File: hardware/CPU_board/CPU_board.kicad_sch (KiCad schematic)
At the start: 109 parts, among them J1 TF TF-018 1.5mm, J2 SOUTH, J3 NORTH, J4 Conn_01x6_Male, J5 Conn_01x03, J6 JTAG, J8 Conn_01x10_Male, U1 EA3036A, U2 W25Q32JVZPIQ, U3 D1s-eLQFP128, U4 PAD30, U5 PAD30, U6 PAD30, U7 PAD30, U8 PAD30, U9 PAD30, X1 24MHz, X2 32.768KHz

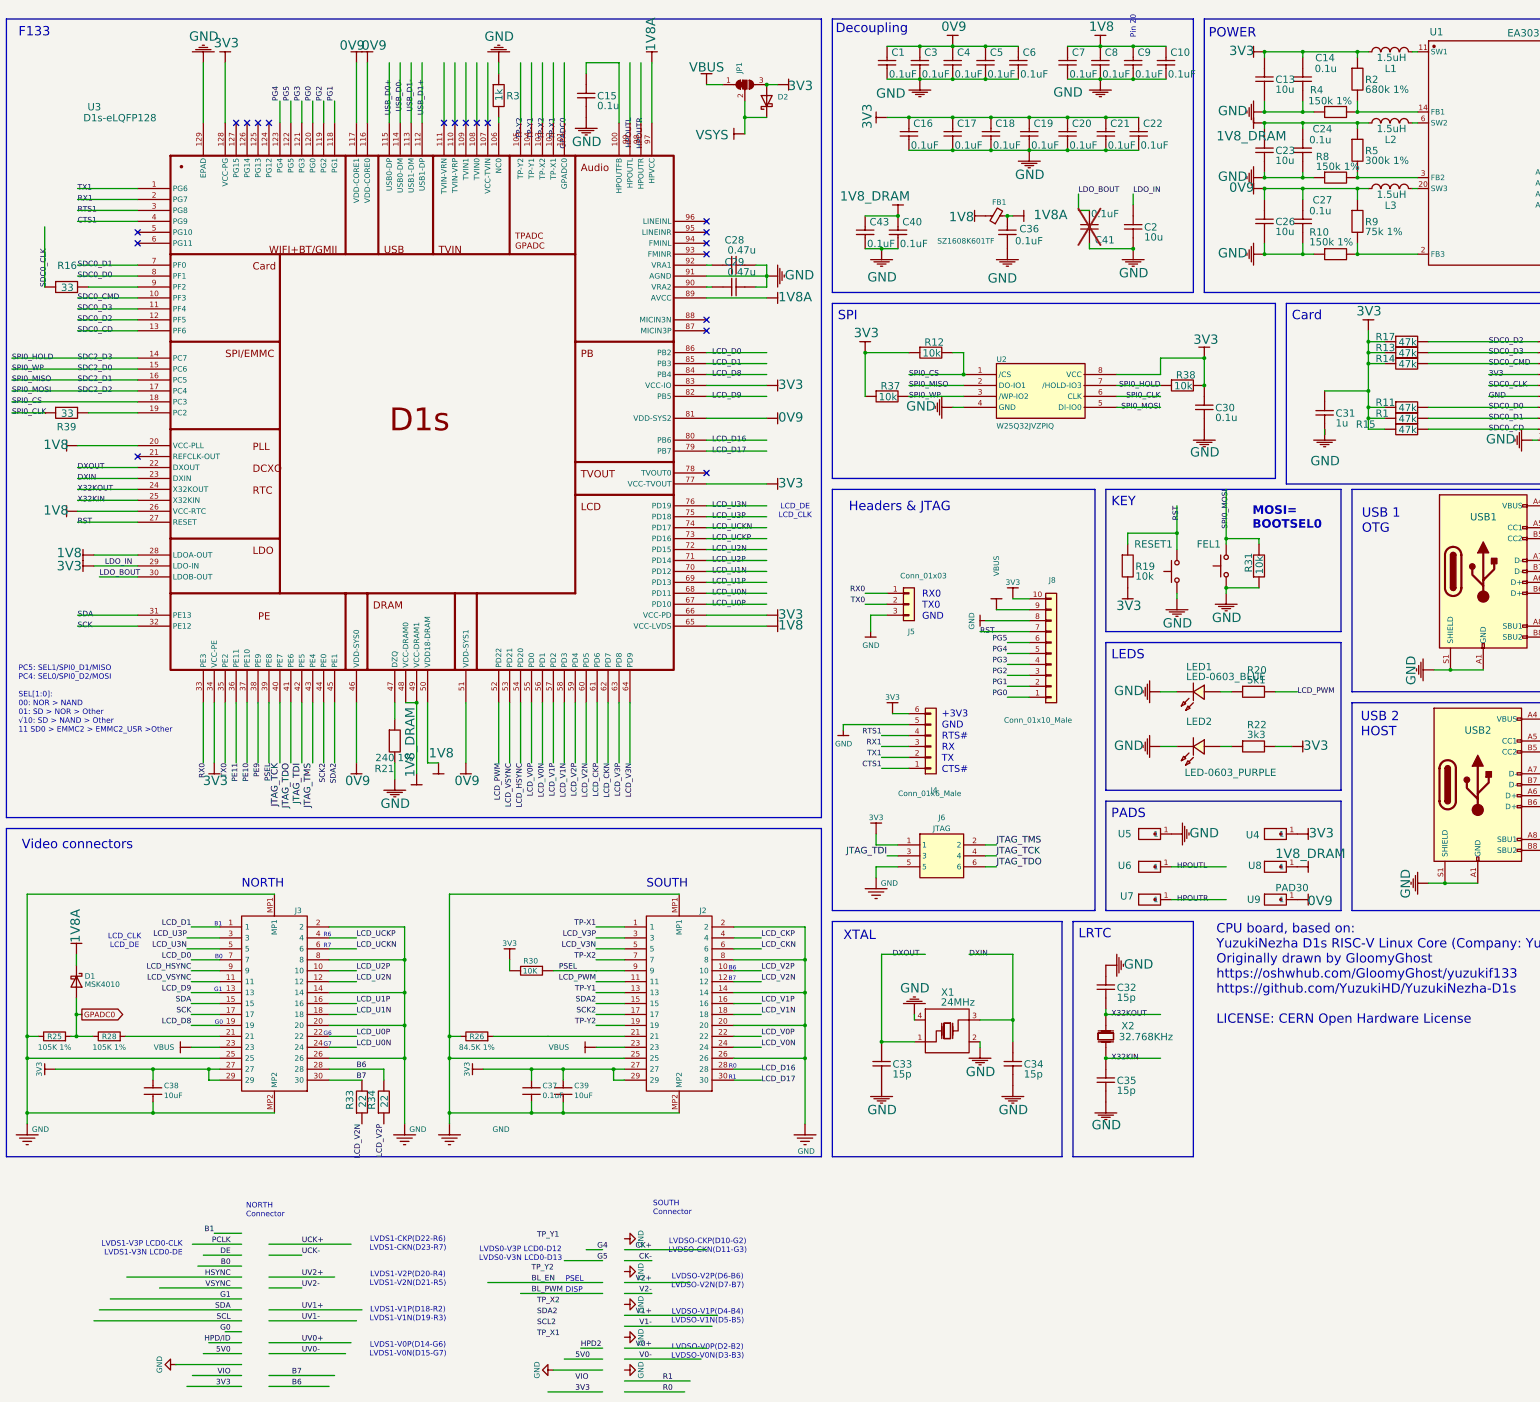
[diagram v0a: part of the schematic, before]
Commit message: fixed mixup of pins G5/G4 (3rd diff pair ODD) and DE/PCLK (3rd diff pair EVEN), now with correct polarity for diff pairs
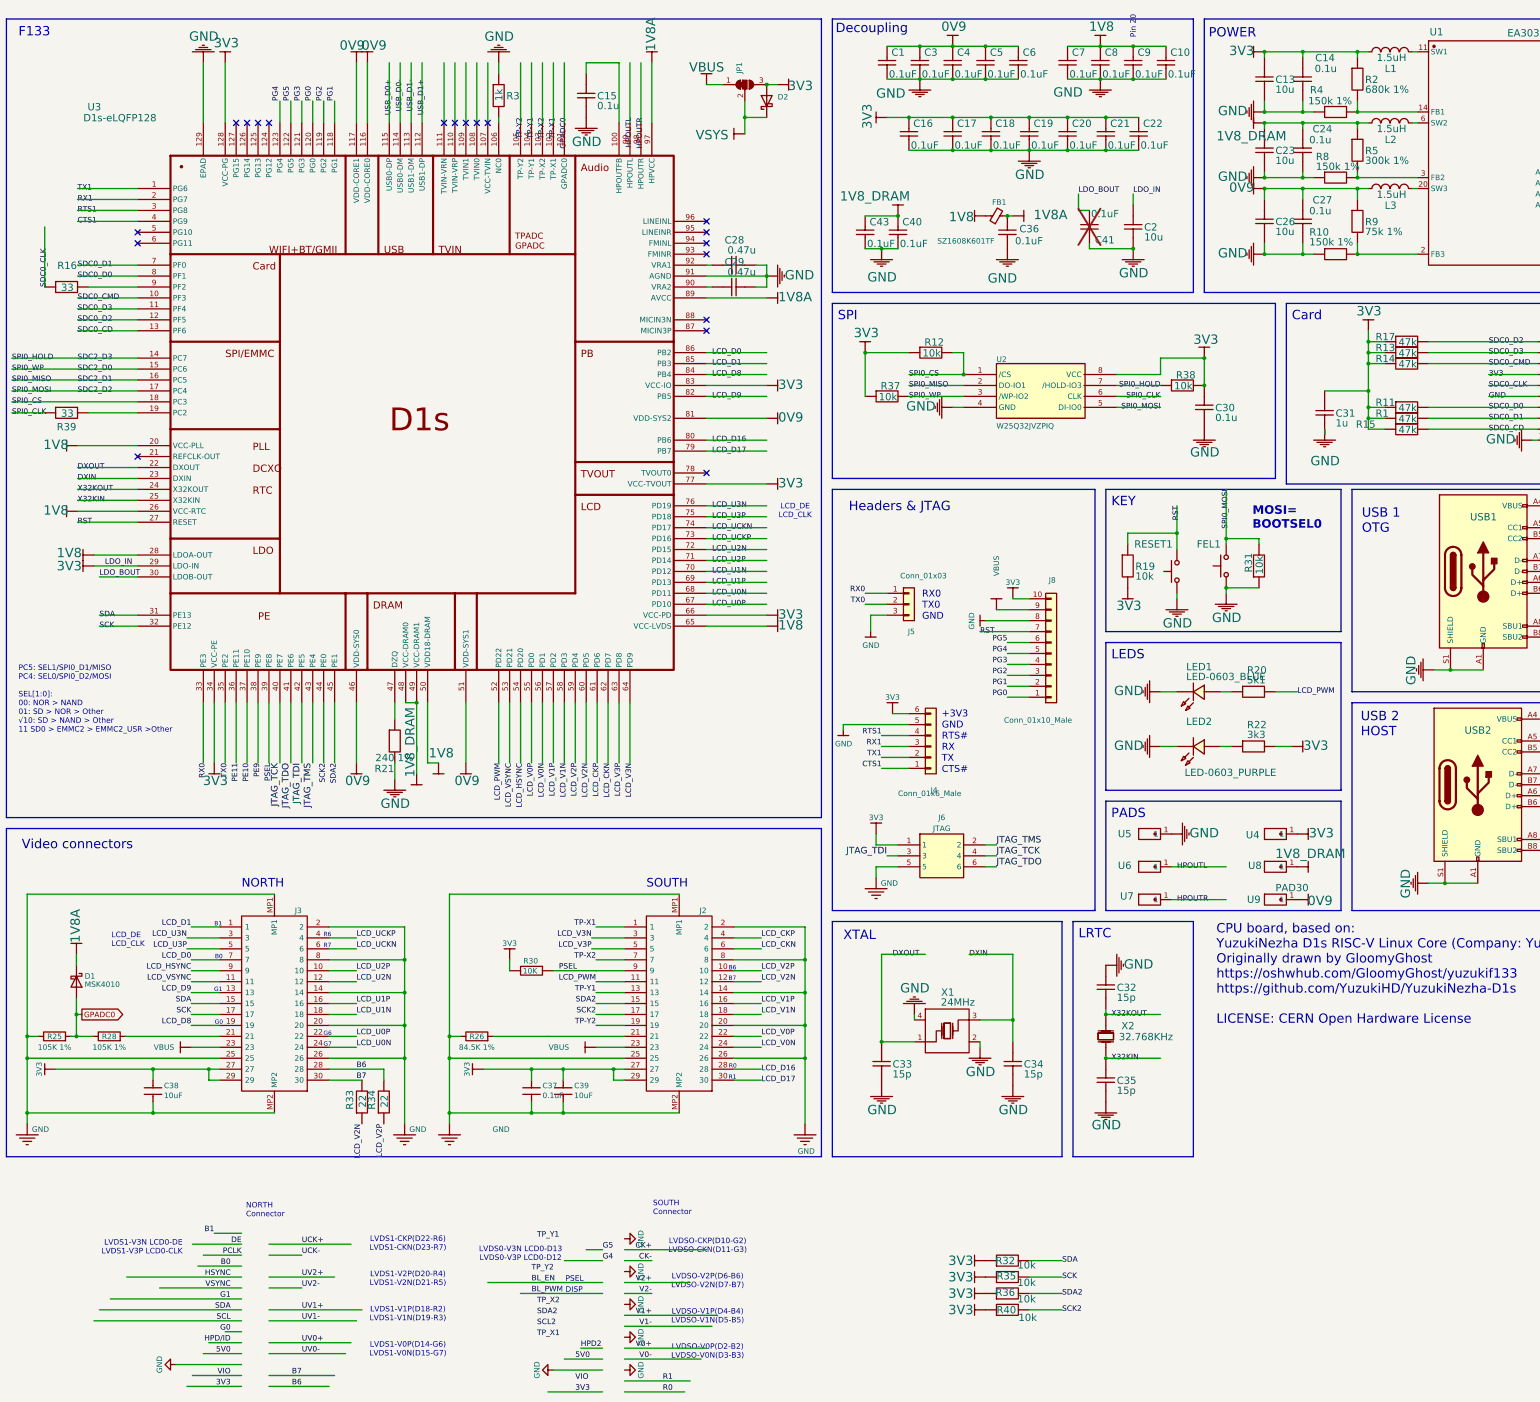
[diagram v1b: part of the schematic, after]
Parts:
- added R32, R35, R36, R40: 10k, Resistor_SMD:R_0402_1005Metric, symbol R_0603_EU_7
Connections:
- net 3V3: now also R32.2, R35.2, R36.2, R40.2
- net LCD_U3N: now also J3.3; no longer J3.5
- net LCD_U3P: now also J3.5; no longer J3.3
- net LCD_V3N: now also J2.3; no longer J2.5
- net LCD_V3P: now also J2.5; no longer J2.3
- net SCK: now also R35.1
- net SCK2: now also R40.1
- net SDA: now also R32.1
- net SDA2: now also R36.1
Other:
- note added: "LVDS0-V3N LCD0-D13 LVDS0-V3P LCD0-D12"
- note added: "LVDS1-V3N LCD0-DE LVDS1-V3P LCD0-CLK"
- note removed: "LCD_CLK LCD_DE"
- note removed: "LVDS0-V3P LCD0-D12 LVDS0-V3N LCD0-D13"
- note removed: "LVDS1-V3P LCD0-CLK LVDS1-V3N LCD0-DE"

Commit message: add JST connector for I2C
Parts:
- removed FEL1: FEL, Button_Switch_SMD:SW_SPST_PTS810, symbol Switch:SW_Push
- removed R11, R13, R17: 47k, Resistor_SMD:R_0402_1005Metric, symbol R_0201_EU_1
- removed R14: 47k, Resistor_SMD:R_0402_1005Metric, symbol R_0201_EU_2
- removed RESET1: RESET, Button_Switch_SMD:SW_SPST_PTS810, symbol Switch:SW_Push
- added CN1: BM04B-SRSS-TB, Connector_JST:JST_SH_BM04B-SRSS-TB_1x04-1MP_P1.00mm_Vertical, symbol Connector_Generic_MountingPin:Conn_01x04_MountingPin
- added JP2: SolderJumper_2_Open, Jumper:SolderJumper-2_P1.3mm_Open_RoundedPad1.0x1.5mm, symbol Jumper:SolderJumper_2_Open
- added RN7: 10K, Resistor_SMD:R_Array_Convex_4x0402, symbol Device:R_Pack04
- added SW1: BOOT, Button_Switch_SMD:SW_Push_SPST_NO_Alps_SKRK, symbol Switch:SW_Push
- added SW2: RESET, Button_Switch_SMD:SW_Push_SPST_NO_Alps_SKRK, symbol Switch:SW_Push
- C12: footprint Capacitor_SMD:C_0603_1608Metric -> Capacitor_SMD:C_0402_1005Metric
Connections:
- net 3V3: now also JP2.1 (A), RN7.1 (R1.1), RN7.2 (R2.1), RN7.3 (R3.1), RN7.4 (R4.1)
- net GND: now also CN1.1 (Pin_1), CN1.MP (MountPin), SW1.2, SW2.2
- net RST: now also SW2.1
- net SCK: now also CN1.4 (Pin_4)
- net SDA: now also CN1.3 (Pin_3)
- net SDC0_CMD: now also R1.2
- net SDC0_D0: now also RN7.7 (R2.2)
- net SDC0_D1: now also RN7.8 (R1.2); no longer R1.2
- net SDC0_D2: now also RN7.5 (R4.2)
- net SDC0_D3: now also RN7.6 (R3.2)
- net SDC2_D2: now also SW1.1
- new net: CN1.2 (Pin_2), JP2.2 (B)
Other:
- moved on the sheet: J4, J5, J6, J8, R1

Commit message: move and add resistor arrayas as pullups for SD, fix R0/R1 mixup
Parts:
- removed R1, R15: 47k, Resistor_SMD:R_0402_1005Metric, symbol R_0201_EU_1
- added RN1: 47K, Resistor_SMD:R_Array_Convex_4x0402, symbol Device:R_Pack04
- RN7: value 10K -> 47K; MPN 4D02WGJ0103TCE -> 4D02WGJ0473TCE
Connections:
- net 3V3: now also RN7.6 (R3.2), RN7.7 (R2.2), RN7.8 (R1.2), RN1.5 (R4.2), RN1.6 (R3.2), RN1.7 (R2.2); no longer RN7.1 (R1.1), RN7.2 (R2.1), RN7.3 (R3.1), RN7.4 (R4.1)
- net SDC0_CD: now also RN1.2 (R2.1)
- net SDC0_CMD: now also RN7.1 (R1.1)
- net SDC0_D0: now also RN1.4 (R4.1); no longer RN7.7 (R2.2)
- net SDC0_D1: now also RN1.3 (R3.1); no longer RN7.8 (R1.2)
- net SDC0_D2: now also RN7.3 (R3.1); no longer RN7.5 (R4.2)
- net SDC0_D3: now also RN7.2 (R2.1); no longer RN7.6 (R3.2)
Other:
- moved on the sheet: C31, J1, RN7

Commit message: fixes for producion and notes
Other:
- note removed: "CPU board, based on: YuzukiNezha D1s RISC-V Linux Core (Company: YuzukiHD) Originally drawn by GloomyGhost https://oshwhub.com/GloomyGhost/yuzukif133 https://github.com/YuzukiHD/YuzukiNezha-D1s LICENSE: CERN Open Hardware License"
- note removed: "DISP"
- note removed: "LVDS0-V3N LCD0-D13 LVDS0-V3P LCD0-D12"
- note removed: "LVDS1-CKP(D22-R6) LVDS1-CKN(D23-R7) LVDS1-V2P(D20-R4) LVDS1-V2N(D21-R5) LVDS1-V1P(D18-R2) LVDS1-V1N(D19-R3) LVDS1-V0P(D14-G6) LVDS1-V0N(D15-G7)"
- note removed: "LVDS1-V3N LCD0-DE LVDS1-V3P LCD0-CLK"
- note removed: "LVDSO-CKP(D10-G2) LVDSO-CKN(D11-G3) LVDSO-V2P(D6-B6) LVDSO-V2N(D7-B7) LVDSO-V1P(D4-B4) LVDSO-V1N(D5-B5) LVDSO-V0P(D2-B2) LVDSO-V0N(D3-B3)"
- note removed: "NORTH Connector"
- note removed: "PSEL"
- note removed: "SEL[1:0] 00: NOR > NAND 01: SD > NOR > Other √10: SD > NAND > Other 11 SD > EMMC2 > EMMC2_USR >Other"
- note removed: "SOUTH Connector"
- note removed: "SPI0 CS/MOSI/MISO has reset PU"
- company: (C) 2023-2024 Victor Suarez Rovere -> (C) 2023-2026 Victor Suarez Rovere
- moved on the sheet: R32, R35, R36, R40
